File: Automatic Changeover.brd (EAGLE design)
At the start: 174 x 152.1 mm, 49 parts, among them IC1 ACS750LCA-050, IC2 XMEGA16A4A, IC4 ACS750LCA-050, IC5 ACS750LCA-050, K1 S216SE1, K2 S216SE1, K3 S216SE1, K4 S216SE1, K5 S216SE1, K6 S216SE1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

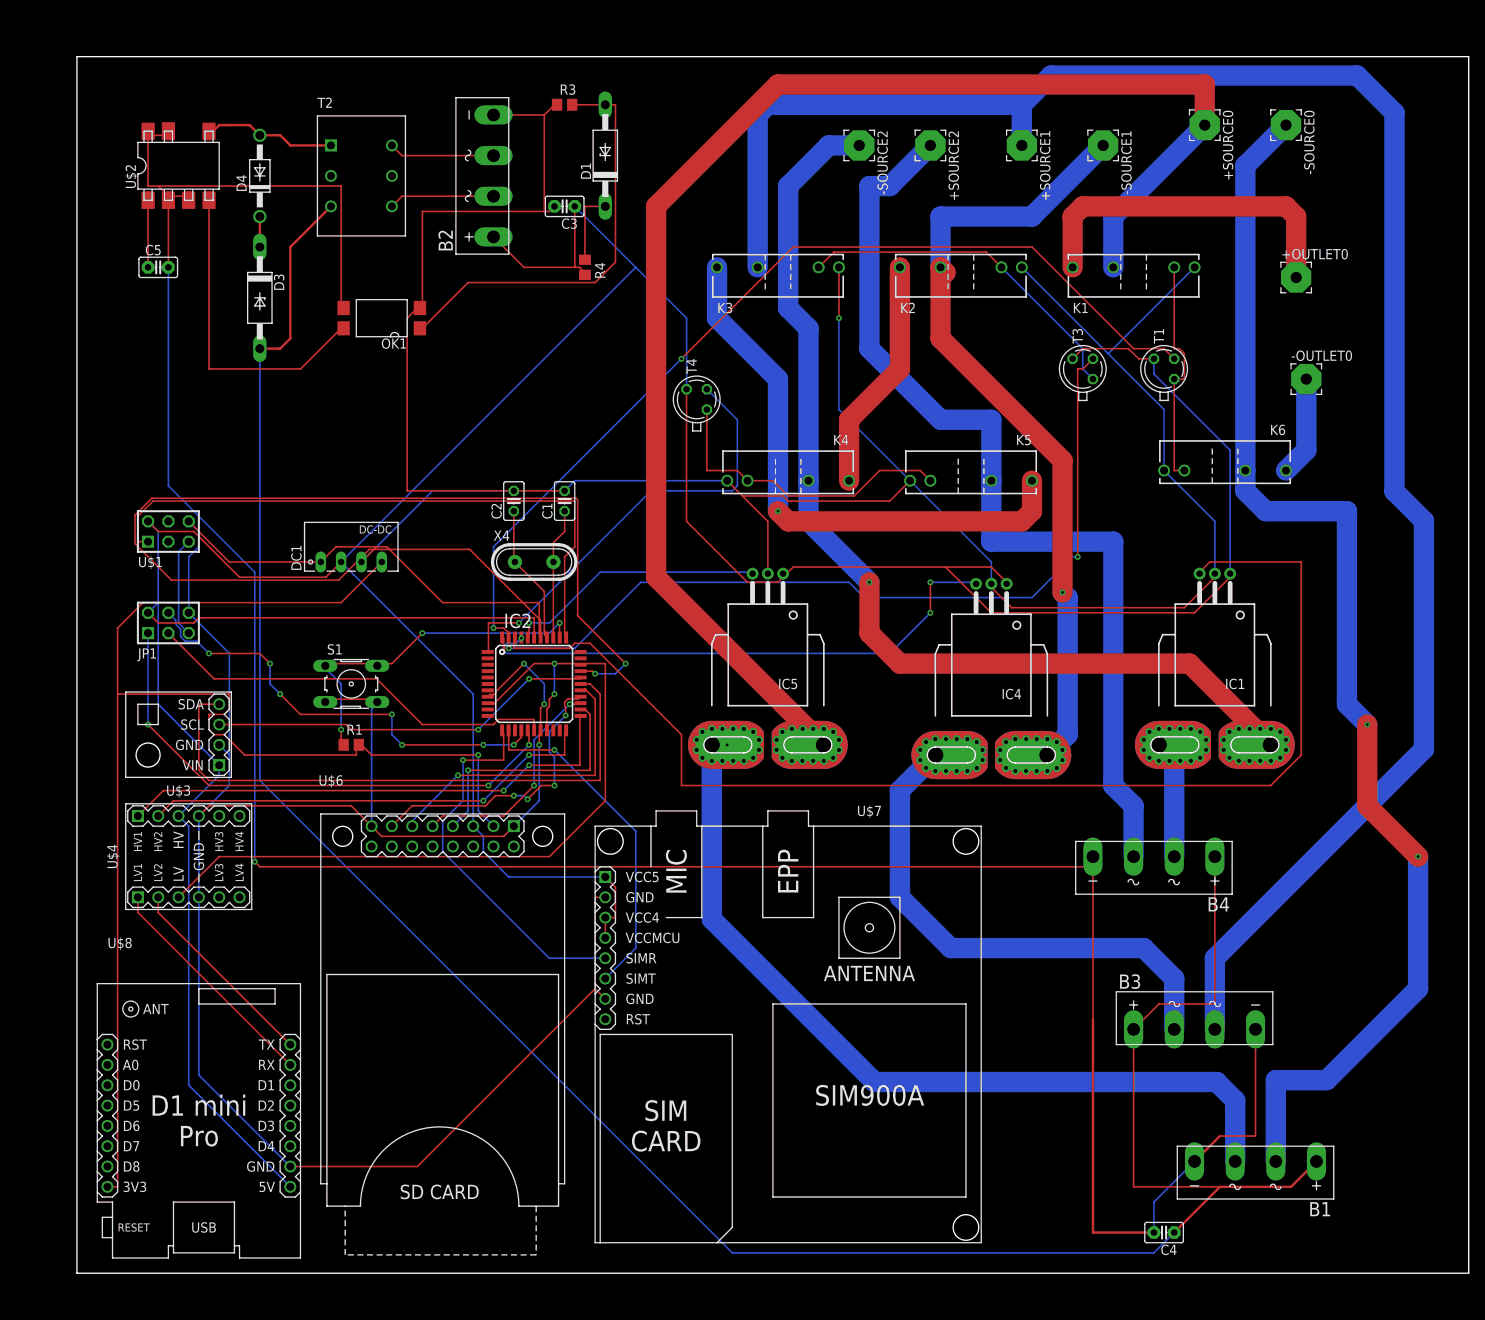
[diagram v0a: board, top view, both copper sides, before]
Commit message: done resizing
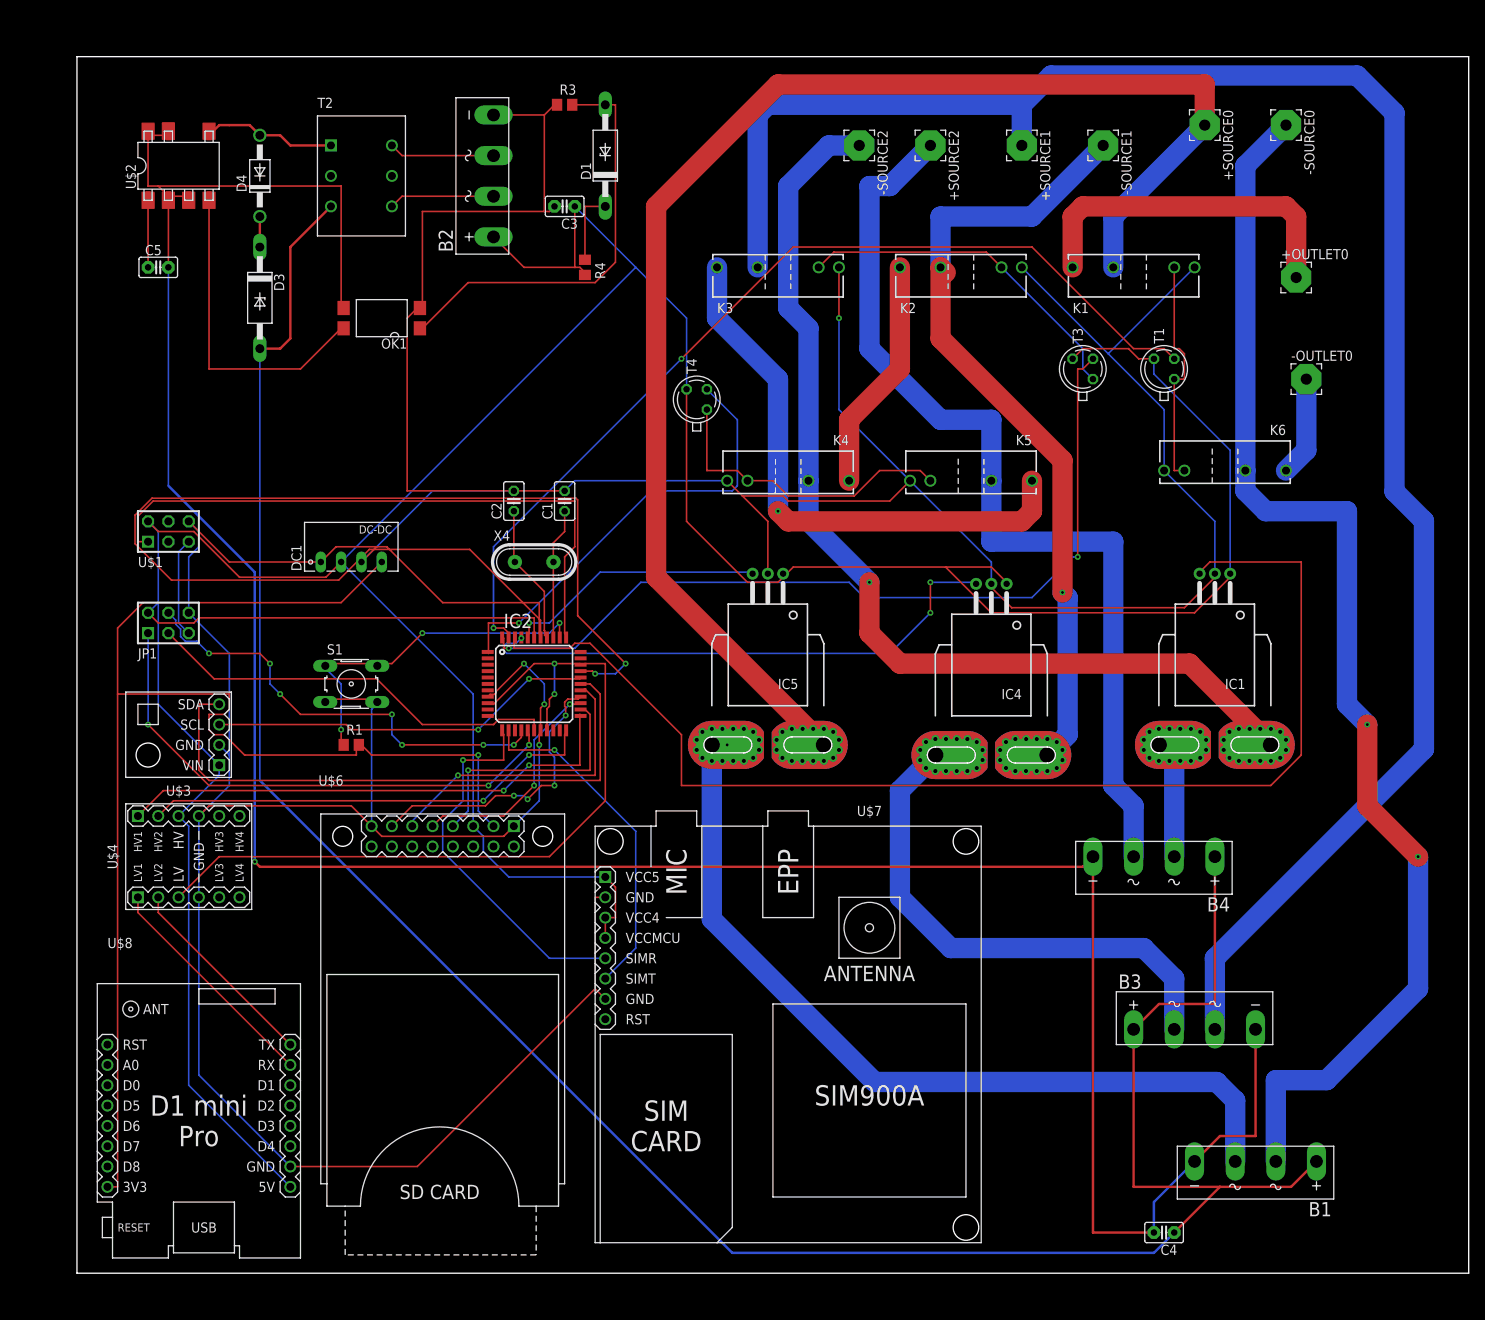
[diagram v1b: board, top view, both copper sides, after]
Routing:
- net N$41: track 333.5 -> 334.0 mm
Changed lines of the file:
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@@
 <wire x1="33.02" y1="120.65" x2="33.33" y2="120.65" width="0.2032" layer="1"/>
 <wire x1="11.43" y1="134.62" x2="11.43" y2="125.73" width="0.2032" layer="1"/>
-<wire x1="134.62" y1="8.89" x2="134.62" y2="5.08" width="0.2032" layer="16"/>
-<wire x1="139.7" y1="13.97" x2="134.62" y2="8.89" width="0.2032" layer="16"/>
-<wire x1="147.32" y1="17.145" x2="147.32" y2="30.48" width="0.2032" layer="1"/>
-<wire x1="142.875" y1="17.145" x2="147.32" y2="17.145" width="0.2032" layer="1"/>
+<wire x1="134.62" y1="8.89" x2="134.62" y2="5.08" width="0.3048" layer="16"/>
+<wire x1="139.7" y1="13.97" x2="134.62" y2="8.89" width="0.3048" layer="16"/>
+<wire x1="147.32" y1="17.145" x2="147.32" y2="30.48" width="0.3048" layer="1"/>
+<wire x1="142.875" y1="17.145" x2="147.32" y2="17.145" width="0.3048" layer="1"/>
 <wire x1="139.7" y1="13.97" x2="142.875" y2="17.145" width="0.3048" layer="1"/>
-<wire x1="127" y1="5.08" x2="127" y2="31.75" width="0.3048" layer="1"/>
-<wire x1="127" y1="50.8" x2="127" y2="31.75" width="0.2032" layer="1"/>
+<wire x1="127" y1="5.08" x2="127" y2="48.26" width="0.3048" layer="1"/>
+<wire x1="127" y1="48.26" x2="127" y2="50.8" width="0.3048" layer="1"/>
 <wire x1="134.62" y1="5.08" x2="127" y2="5.08" width="0.3048" layer="1"/>
 <wire x1="11.43" y1="98.425" x2="11.43" y2="125.73" width="0.2032" layer="16"/>
-<wire x1="22.225" y1="87.63" x2="11.43" y2="98.425" width="0.2032" layer="16"/>
-<wire x1="22.225" y1="51.435" x2="22.225" y2="87.63" width="0.2032" layer="16"/>
-<wire x1="22.86" y1="50.8" x2="22.225" y2="51.435" width="0.2032" layer="1"/>
-<wire x1="127" y1="50.8" x2="22.86" y2="50.8" width="0.2032" layer="1"/>
-<wire x1="127" y1="50.8" x2="127" y2="52.07" width="0.2032" layer="1"/>
+<wire x1="22.225" y1="87.63" x2="11.43" y2="98.425" width="0.3048" layer="16"/>
+<wire x1="22.225" y1="51.435" x2="22.225" y2="87.63" width="0.3048" layer="16"/>
+<wire x1="125.73" y1="50.8" x2="22.86" y2="50.8" width="0.3048" layer="1"/>
+<wire x1="22.86" y1="50.8" x2="22.225" y2="51.435" width="0.3048" layer="1"/>
+<wire x1="127" y1="52.07" x2="125.73" y2="50.8" width="0.3048" layer="1"/>
 <via x="22.225" y="51.435" extent="1-16" drill="0.35"/>
 <wire x1="13.97" y1="134.62" x2="11.43" y2="134.62" width="0.2032" layer="1"/>
@@
 <wire x1="11.412221875" y1="142.24" x2="11.419840625" y2="142.23238125" width="0.2032" layer="1"/>
 <wire x1="11.43" y1="142.24" x2="11.412221875" y2="142.24" width="0.2032" layer="1"/>
+<wire x1="127" y1="52.07" x2="127" y2="50.8" width="0.3048" layer="1"/>
 </signal>
 <signal name="N$38">
@@
 <wire x1="151.765" y1="10.795" x2="142.875" y2="10.795" width="0.3048" layer="1"/>
 <wire x1="154.94" y1="13.97" x2="151.765" y2="10.795" width="0.3048" layer="1"/>
-<wire x1="132.08" y1="10.795" x2="132.08" y2="30.48" width="0.2032" layer="1"/>
-<wire x1="142.875" y1="10.795" x2="132.08" y2="10.795" width="0.2032" layer="1"/>
-<wire x1="142.24" y1="33.655" x2="142.24" y2="52.07" width="0.2032" layer="1"/>
-<wire x1="135.255" y1="33.655" x2="142.24" y2="33.655" width="0.2032" layer="1"/>
-<wire x1="132.08" y1="30.48" x2="135.255" y2="33.655" width="0.2032" layer="1"/>
+<wire x1="132.08" y1="10.795" x2="132.08" y2="30.48" width="0.3048" layer="1"/>
+<wire x1="142.875" y1="10.795" x2="132.08" y2="10.795" width="0.3048" layer="1"/>
+<wire x1="142.24" y1="33.655" x2="142.24" y2="52.07" width="0.3048" layer="1"/>
+<wire x1="135.255" y1="33.655" x2="142.24" y2="33.655" width="0.3048" layer="1"/>
+<wire x1="132.08" y1="30.48" x2="135.255" y2="33.655" width="0.3048" layer="1"/>
 <wire x1="22.86" y1="61.595" x2="22.86" y2="115.57" width="0.2032" layer="16"/>
-<wire x1="81.915" y1="2.54" x2="22.86" y2="61.595" width="0.2032" layer="16"/>
-<wire x1="134.62" y1="2.54" x2="81.915" y2="2.54" width="0.2032" layer="16"/>
-<wire x1="137.16" y1="5.08" x2="134.62" y2="2.54" width="0.2032" layer="16"/>
+<wire x1="81.915" y1="2.54" x2="22.86" y2="61.595" width="0.3048" layer="16"/>
+<wire x1="134.62" y1="2.54" x2="81.915" y2="2.54" width="0.3048" layer="16"/>
+<wire x1="137.16" y1="5.08" x2="134.62" y2="2.54" width="0.3048" layer="16"/>
 </signal>
 <signal name="N$14">

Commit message: a few important refinement
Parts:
- moved T4 1.27 mm to (78.7, 109.2)
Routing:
- net GND: track 768.7 -> 713.7 mm, vias 6 -> 7
- net IN2: track 150.3 -> 166.0 mm
- net +5V: track 491.2 -> 498.1 mm
- net 3V3: track 174.6 -> 170.0 mm, vias 1 -> 3
- net +SOURCE1: track 234.6 -> 238.8 mm
- net N$41: track 334.0 -> 337.2 mm
- net MISO: track 66.2 -> 69.1 mm
- net N$20: track 64.5 -> 61.5 mm
- net PDI_DATA: track 77.5 -> 80.0 mm
- net N$58: track 28.8 -> 31.3 mm
- net N$17: track 298.6 -> 296.3 mm
- net OUT0: track 119.3 -> 121.4 mm
- net N$63: track 38.7 -> 37.4 mm
- net RX_WIFI_BRD: track 28.8 -> 29.6 mm
- net OUT2: track 55.9 -> 55.4 mm
